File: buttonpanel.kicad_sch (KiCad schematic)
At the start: 10 parts, among them SW1 SW_Push, SW5 SW_Push

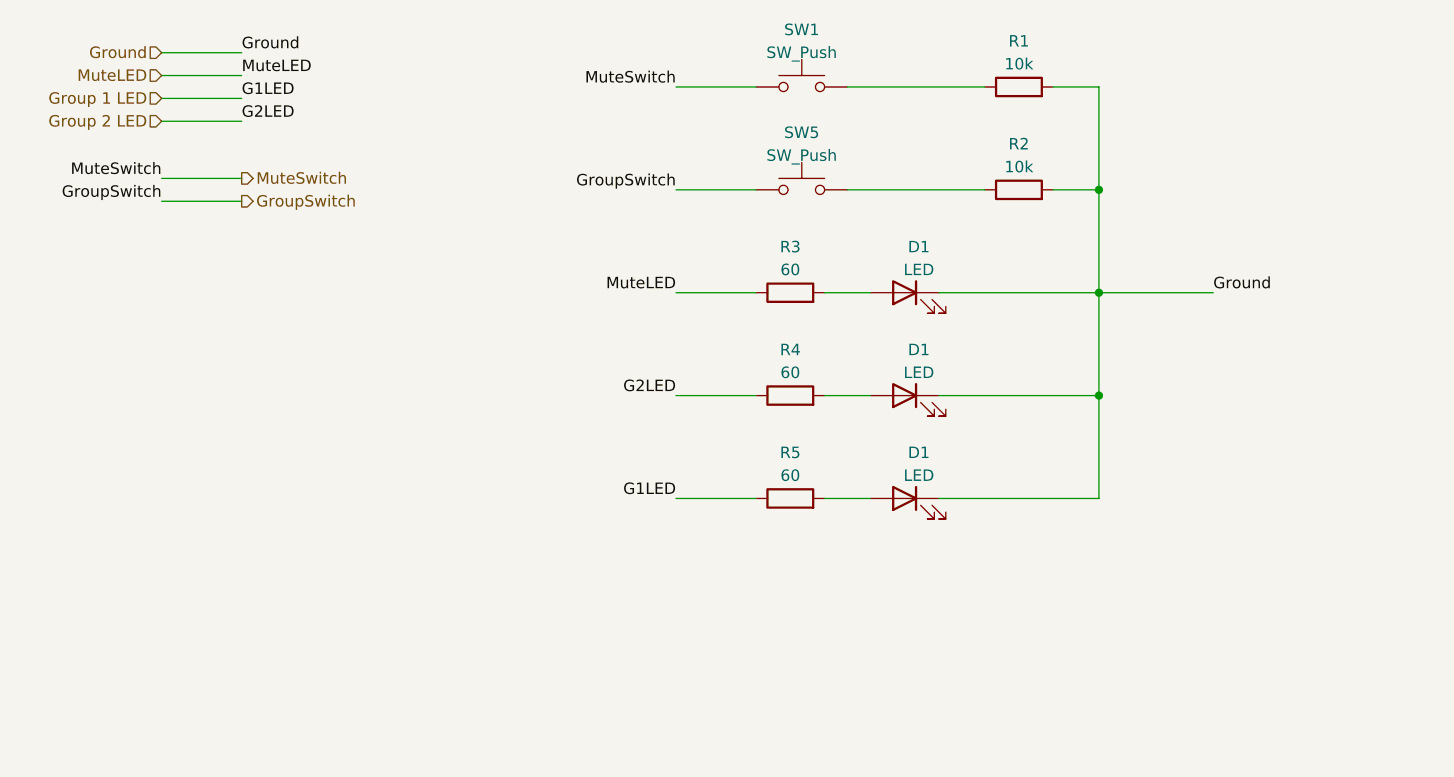
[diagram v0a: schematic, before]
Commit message: Finished up schematic, before board splitting
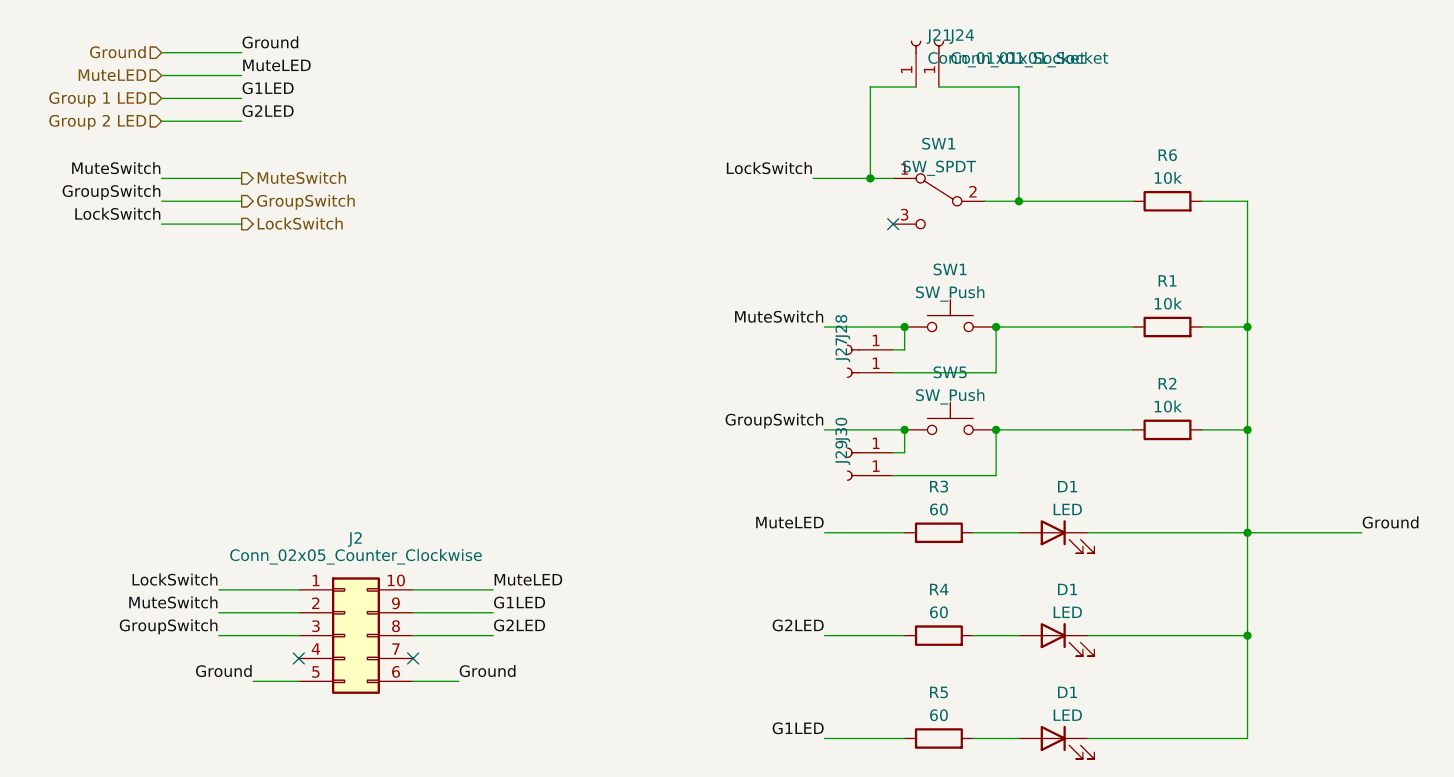
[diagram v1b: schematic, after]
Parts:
- added J2: Conn_02x05_Counter_Clockwise, Connector_PinSocket_2.54mm:PinSocket_2x05_P2.54mm_Vertical, symbol Connector_Generic:Conn_02x05_Counter_Clockwise
- added J21, J24, J27, J28, J29, J30: Conn_01x01_Socket, Connector_Wire:SolderWire-0.75sqmm_1x01_D1.25mm_OD2.3mm, symbol Connector:Conn_01x01_Socket
- added R6: 10k, Resistor_SMD:R_0805_2012Metric, symbol Device:R
- added SW1: SW_SPDT, symbol Switch:SW_SPDT
- D1: footprint (none) -> LED_THT:LED_D5.0mm
- R1, R2, R3, R4, R5: footprint (none) -> Resistor_SMD:R_0805_2012Metric
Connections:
- net Ground: now also J2.5 (Pin_5), J2.6 (Pin_6), R6.2
- net Group 1 LED: now also J2.9 (Pin_9)
- net Group 2 LED: now also J2.8 (Pin_8)
- net GroupSwitch: now also J2.3 (Pin_3), J30.1 (Pin_1)
- net MuteLED: now also J2.10 (Pin_10)
- net MuteSwitch: now also J2.2 (Pin_2), J28.1 (Pin_1)
- net at R2.1, SW5.2: now also J29.1 (Pin_1)
- net at R1.1, SW1.2: now also J27.1 (Pin_1)
- new net: J24.1 (Pin_1), R6.1, SW1.2 (B)
- new net LockSwitch: J2.1 (Pin_1), J21.1 (Pin_1), SW1.1 (A)
- no-connect marks 0 -> 3
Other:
- moved on the sheet: D1, R1, R2, R3, R4, R5, SW1, SW5

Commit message: Changed position of ribbon connectors, added DC
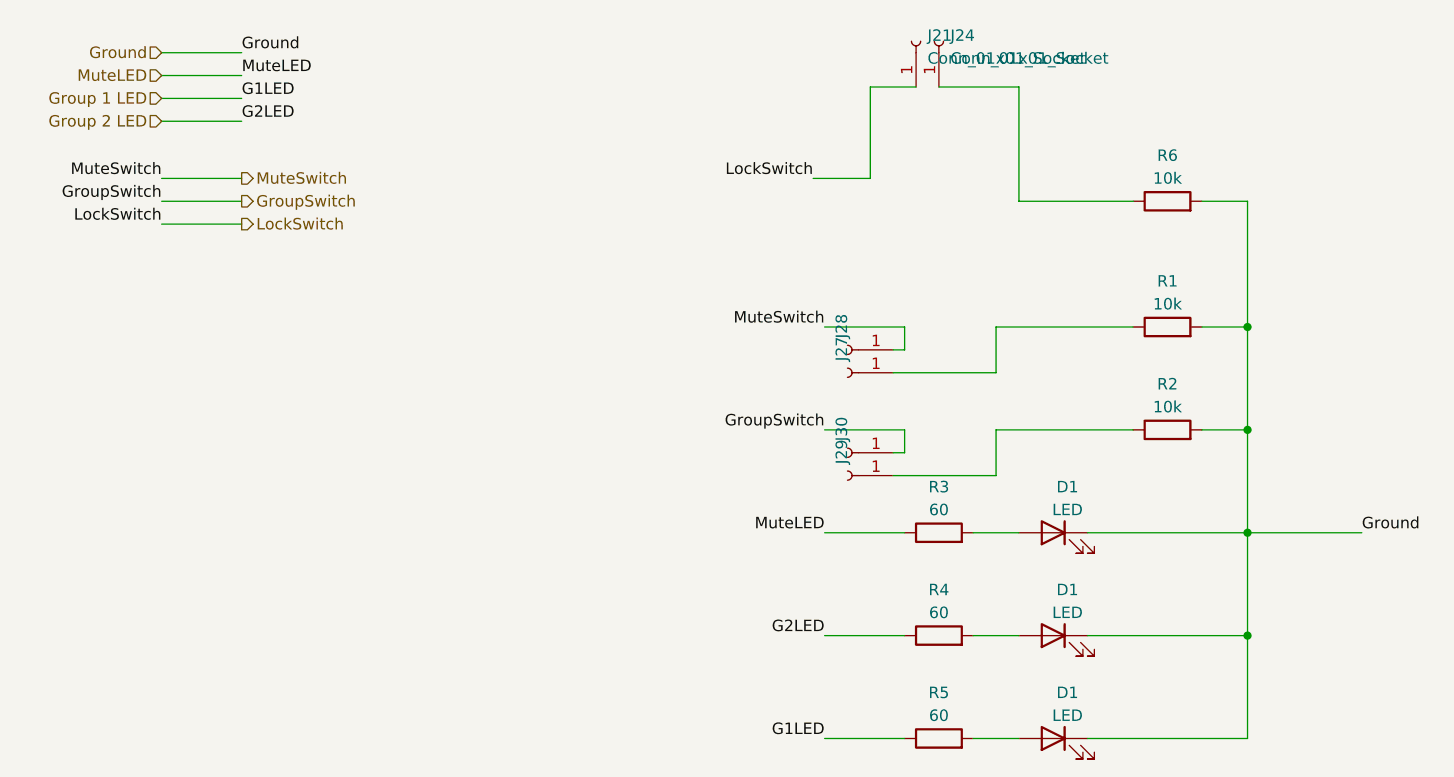
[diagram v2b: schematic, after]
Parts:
- removed J2: Conn_02x05_Counter_Clockwise, Connector_PinSocket_2.54mm:PinSocket_2x05_P2.54mm_Vertical, symbol Connector_Generic:Conn_02x05_Counter_Clockwise
- removed SW1, SW5: SW_Push, symbol Switch:SW_Push
- removed SW1: SW_SPDT, symbol Switch:SW_SPDT
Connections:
- no-connect marks 3 -> 0
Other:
- company: (none) -> Daniel Machnik Sounddesign und Tontechnik
- title: (none) -> Essigfabrik 2-Way PA Switcher
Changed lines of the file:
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@@
 (kicad_sch (version 20230121) (generator eeschema)
   (paper "A4")
+  (title_block
+    (title "Essigfabrik 2-Way PA Switcher")
+    (date "2023-11-21")
+    (rev "1")
+    (company "Daniel Machnik Sounddesign und Tontechnik")
+  )
   (junction (at 156.21 95.25) (diameter 0) (color 0 0 0 0)
   )
-  (junction (at 130.81 46.99) (diameter 0) (color 0 0 0 0)
-  )
-  (junction (at 118.11 60.96) (diameter 0) (color 0 0 0 0)
-  )
-  (junction (at 128.27 72.39) (diameter 0) (color 0 0 0 0)
-  )
-  (junction (at 118.11 72.39) (diameter 0) (color 0 0 0 0)
-  )
-  (junction (at 114.3 44.45) (diameter 0) (color 0 0 0 0)
-  )
   (junction (at 156.21 72.39) (diameter 0) (color 0 0 0 0)
   )
@@
   (junction (at 156.21 60.96) (diameter 0) (color 0 0 0 0)
   )
-  (junction (at 128.27 60.96) (diameter 0) (color 0 0 0 0)
-  )
-  (no_connect (at 63.5 97.79))
-  (no_connect (at 116.84 49.53))
-  (no_connect (at 50.8 97.79))
   (wire (pts (xy 128.27 72.39) (xy 143.51 72.39))
     (stroke (width 0) (type default))
@@
     (stroke (width 0) (type default))
   )
-  (wire (pts (xy 41.91 90.17) (xy 50.8 90.17))
-    (stroke (width 0) (type default))
-  )
   (wire (pts (xy 109.22 72.39) (xy 118.11 72.39))
     (stroke (width 0) (type default))
@@
     (stroke (width 0) (type default))
   )
-  (wire (pts (xy 41.91 95.25) (xy 50.8 95.25))
-    (stroke (width 0) (type default))
-  )
   (wire (pts (xy 156.21 60.96) (xy 156.21 72.39))
     (stroke (width 0) (type default))
@@
     (stroke (width 0) (type default))
   )
-  (wire (pts (xy 63.5 100.33) (xy 68.58 100.33))
-    (stroke (width 0) (type default))
-  )
-  (wire (pts (xy 63.5 90.17) (xy 72.39 90.17))
-    (stroke (width 0) (type default))
-  )
   (wire (pts (xy 35.56 49.53) (xy 44.45 49.53))
     (stroke (width 0) (type default))
@@
     (stroke (width 0) (type default))
   )
-  (wire (pts (xy 50.8 100.33) (xy 45.72 100.33))
-    (stroke (width 0) (type default))
-  )
   (wire (pts (xy 156.21 83.82) (xy 168.91 83.82))
     (stroke (width 0) (type default))
@@
     (stroke (width 0) (type default))
   )
-  (wire (pts (xy 114.3 44.45) (xy 116.84 44.45))
-    (stroke (width 0) (type default))
-  )
   (wire (pts (xy 35.56 35.56) (xy 44.45 35.56))
     (stroke (width 0) (type default))
   )
-  (wire (pts (xy 127 46.99) (xy 130.81 46.99))
-    (stroke (width 0) (type default))
-  )
-  (wire (pts (xy 63.5 92.71) (xy 72.39 92.71))
-    (stroke (width 0) (type default))
-  )
-  (wire (pts (xy 63.5 95.25) (xy 72.39 95.25))
-    (stroke (width 0) (type default))
-  )
   (wire (pts (xy 107.95 44.45) (xy 114.3 44.45))
-    (stroke (width 0) (type default))
-  )
-  (wire (pts (xy 41.91 92.71) (xy 50.8 92.71))
     (stroke (width 0) (type default))
   )
@@
     (effects (font (size 1.27 1.27)) (justify right bottom))
   )
-  (label "Ground" (at 45.72 100.33 180) (fields_autoplaced)
-    (effects (font (size 1.27 1.27)) (justify right bottom))
-  )
   (label "G1LED" (at 109.22 106.68 180) (fields_autoplaced)
     (effects (font (size 1.27 1.27)) (justify right bottom))
@@
     (effects (font (size 1.27 1.27)) (justify left bottom))
   )
-  (label "Ground" (at 68.58 100.33 0) (fields_autoplaced)
-    (effects (font (size 1.27 1.27)) (justify left bottom))
-  )
   (label "GroupSwitch" (at 109.22 72.39 180) (fields_autoplaced)
     (effects (font (size 1.27 1.27)) (justify right bottom))
@@
     (effects (font (size 1.27 1.27)) (justify left bottom))
   )
-  (label "GroupSwitch" (at 41.91 95.25 180) (fields_autoplaced)
-    (effects (font (size 1.27 1.27)) (justify right bottom))
-  )
-  (label "LockSwitch" (at 41.91 90.17 180) (fields_autoplaced)
-    (effects (font (size 1.27 1.27)) (justify right bottom))
-  )
-  (label "G2LED" (at 72.39 95.25 0) (fields_autoplaced)
-    (effects (font (size 1.27 1.27)) (justify left bottom))
-  )
-  (label "MuteLED" (at 72.39 90.17 0) (fields_autoplaced)
-    (effects (font (size 1.27 1.27)) (justify left bottom))
-  )
   (label "MuteLED" (at 44.45 33.02 0) (fields_autoplaced)
     (effects (font (size 1.27 1.27)) (justify left bottom))
   )
-  (label "MuteSwitch" (at 41.91 92.71 180) (fields_autoplaced)
-    (effects (font (size 1.27 1.27)) (justify right bottom))
-  )
-  (label "G1LED" (at 72.39 92.71 0) (fields_autoplaced)
-    (effects (font (size 1.27 1.27)) (justify left bottom))
-  )
   (hierarchical_label "MuteSwitch" (shape output) (at 44.45 44.45 0) (fields_autoplaced)
     (effects (font (size 1.27 1.27)) (justify left))
@@
     )
   )
-  (symbol (lib_id "Switch:SW_Push") (at 123.19 60.96 0) (unit 1)
-    (in_bom yes) (on_board yes) (dnp no) (fields_autoplaced)
-    (property "Reference" "SW1" (at 123.19 54.61 0)
-      (effects (font (size 1.27 1.27)))
-    )
-    (property "Value" "SW_Push" (at 123.19 57.15 0)
-      (effects (font (size 1.27 1.27)))
-    )
-    (property "Footprint" "" (at 123.19 55.88 0)
-      (effects (font (size 1.27 1.27)) hide)
-    )
-    (property "Datasheet" "~" (at 123.19 55.88 0)
-      (effects (font (size 1.27 1.27)) hide)
-    )
-    (pin "1")
-    (pin "2")
-    (instances
-      (project "EF_matrix"
-        (path "/621f65ee-d66d-40b7-9a89-3052b9373190/b97d10d9-dc84-4d90-b1cc-f43ccd4b156b"
-          (reference "SW1") (unit 1)
-        )
-      )
-    )
-  )
   (symbol (lib_id "Connector:Conn_01x01_Socket") (at 121.92 29.21 90) (unit 1)
     (in_bom yes) (on_board yes) (dnp no) (fields_autoplaced)
@@
         (path "/621f65ee-d66d-40b7-9a89-3052b9373190/b97d10d9-dc84-4d90-b1cc-f43ccd4b156b"
           (reference "J24") (unit 1)
-        )
-      )
-    )
-  )
-  (symbol (lib_id "Connector_Generic:Conn_02x05_Counter_Clockwise") (at 55.88 95.25 0) (unit 1)
-    (in_bom yes) (on_board yes) (dnp no)
-    (property "Reference" "J2" (at 57.15 84.455 0)
-      (effects (font (size 1.27 1.27)))
-    )
-    (property "Value" "Conn_02x05_Counter_Clockwise" (at 57.15 86.36 0)
-      (effects (font (size 1.27 1.27)))
-    )
-    (property "Footprint" "Connector_PinSocket_2.54mm:PinSocket_2x05_P2.54mm_Vertical" (at 55.88 95.25 0)
-      (effects (font (size 1.27 1.27)) hide)
-    )
-    (property "Datasheet" "~" (at 55.88 95.25 0)
-      (effects (font (size 1.27 1.27)) hide)
-    )
-    (pin "1")
-    (pin "10")
-    (pin "2")
-    (pin "3")
-    (pin "4")
-    (pin "5")
-    (pin "6")
-    (pin "7")
-    (pin "8")
-    (pin "9")
-    (instances
-      (project "EF_matrix"
-        (path "/621f65ee-d66d-40b7-9a89-3052b9373190/d94772af-2feb-48c7-98be-bb0e397012c8"
-          (reference "J2") (unit 1)
-        )
-        (path "/621f65ee-d66d-40b7-9a89-3052b9373190"
-          (reference "J19") (unit 1)
-        )
-        (path "/621f65ee-d66d-40b7-9a89-3052b9373190/b97d10d9-dc84-4d90-b1cc-f43ccd4b156b"
-          (reference "J20") (unit 1)
         )
       )
@@
     )
   )
-  (symbol (lib_id "Switch:SW_Push") (at 123.19 72.39 0) (unit 1)
-    (in_bom yes) (on_board yes) (dnp no) (fields_autoplaced)
-    (property "Reference" "SW5" (at 123.19 66.04 0)
-      (effects (font (size 1.27 1.27)))
-    )
-    (property "Value" "SW_Push" (at 123.19 68.58 0)
-      (effects (font (size 1.27 1.27)))
-    )
-    (property "Footprint" "" (at 123.19 67.31 0)
-      (effects (font (size 1.27 1.27)) hide)
-    )
-    (property "Datasheet" "~" (at 123.19 67.31 0)
-      (effects (font (size 1.27 1.27)) hide)
-    )
-    (pin "1")
-    (pin "2")
-    (instances
-      (project "EF_matrix"
-        (path "/621f65ee-d66d-40b7-9a89-3052b9373190/b97d10d9-dc84-4d90-b1cc-f43ccd4b156b"
-          (reference "SW5") (unit 1)
-        )
-      )
-    )
-  )
   (symbol (lib_id "Connector:Conn_01x01_Socket") (at 111.76 66.04 180) (unit 1)
     (in_bom yes) (on_board yes) (dnp no) (fields_autoplaced)
@@
         )
       )
-    )
-  )
-  (symbol (lib_id "Switch:SW_SPDT") (at 121.92 46.99 0) (mirror y) (unit 1)
-    (in_bom yes) (on_board yes) (dnp no)
-    (property "Reference" "SW1" (at 121.92 40.64 0)
-      (effects (font (size 1.27 1.27)))
-    )
-    (property "Value" "SW_SPDT" (at 121.92 43.18 0)
-      (effects (font (size 1.27 1.27)))
-    )
-    (property "Footprint" "" (at 121.92 46.99 0)
-      (effects (font (size 1.27 1.27)) hide)
-    )
-    (property "Datasheet" "~" (at 121.92 46.99 0)
-      (effects (font (size 1.27 1.27)) hide)
-    )
-    (pin "1")
-    (pin "2")
-    (pin "3")
-    (instances
-      (project "EF_matrix"
-        (path "/621f65ee-d66d-40b7-9a89-3052b9373190"
-          (reference "SW1") (unit 1)
-        )
-        (path "/621f65ee-d66d-40b7-9a89-3052b9373190/837cbbaa-ad41-4de8-bb02-f85faf12da13"
-          (reference "SW2") (unit 1)
-        )
-        (path "/621f65ee-d66d-40b7-9a89-3052b9373190/64851fbd-c688-4197-a63d-3dce17468ba2"
-          (reference "SW3") (unit 1)
-        )
-        (path "/621f65ee-d66d-40b7-9a89-3052b9373190/b97d10d9-dc84-4d90-b1cc-f43ccd4b156b"
-          (reference "SW6") (unit 1)
-        )
-      )
